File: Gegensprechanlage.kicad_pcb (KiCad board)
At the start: 2 copper layers, 42.2 x 31 mm, 13 parts, among them J1 To other, P1 22k, SW1 SW_Push, U1 LM386

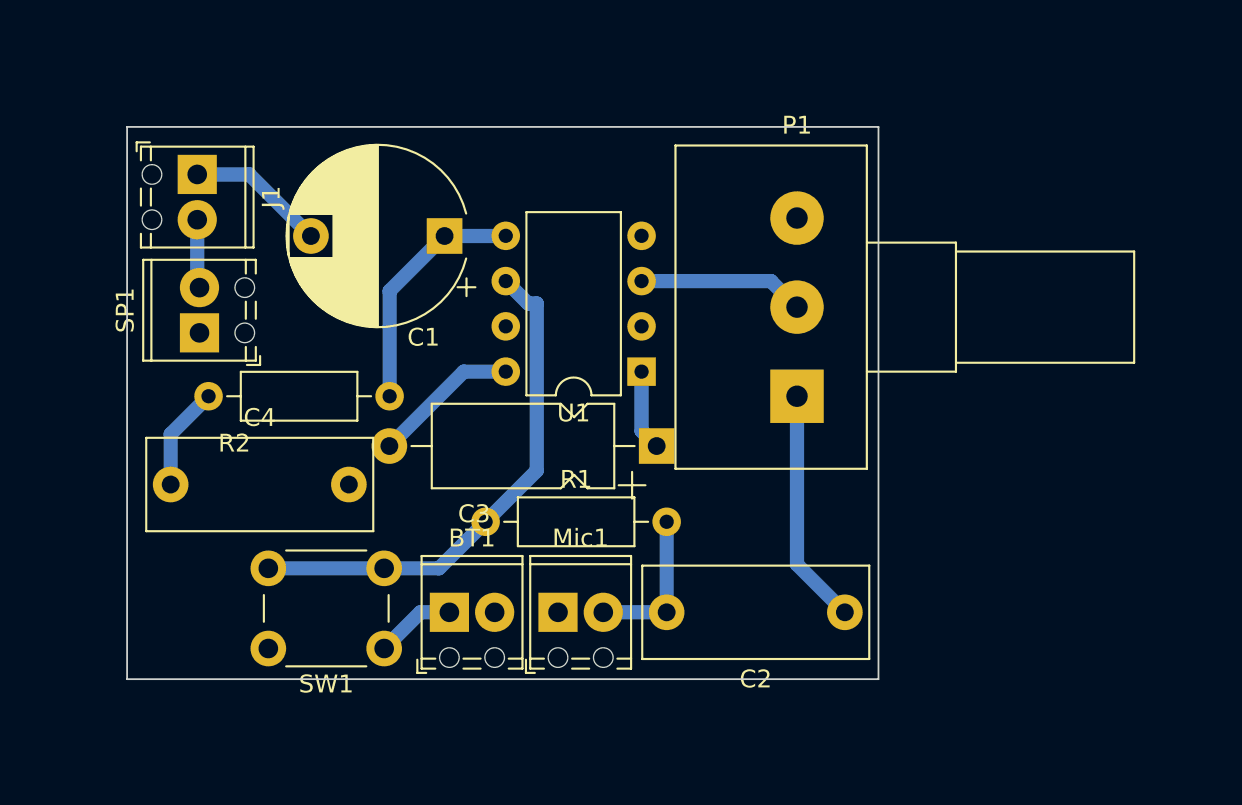
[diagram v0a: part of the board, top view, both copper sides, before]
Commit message: More compact layout
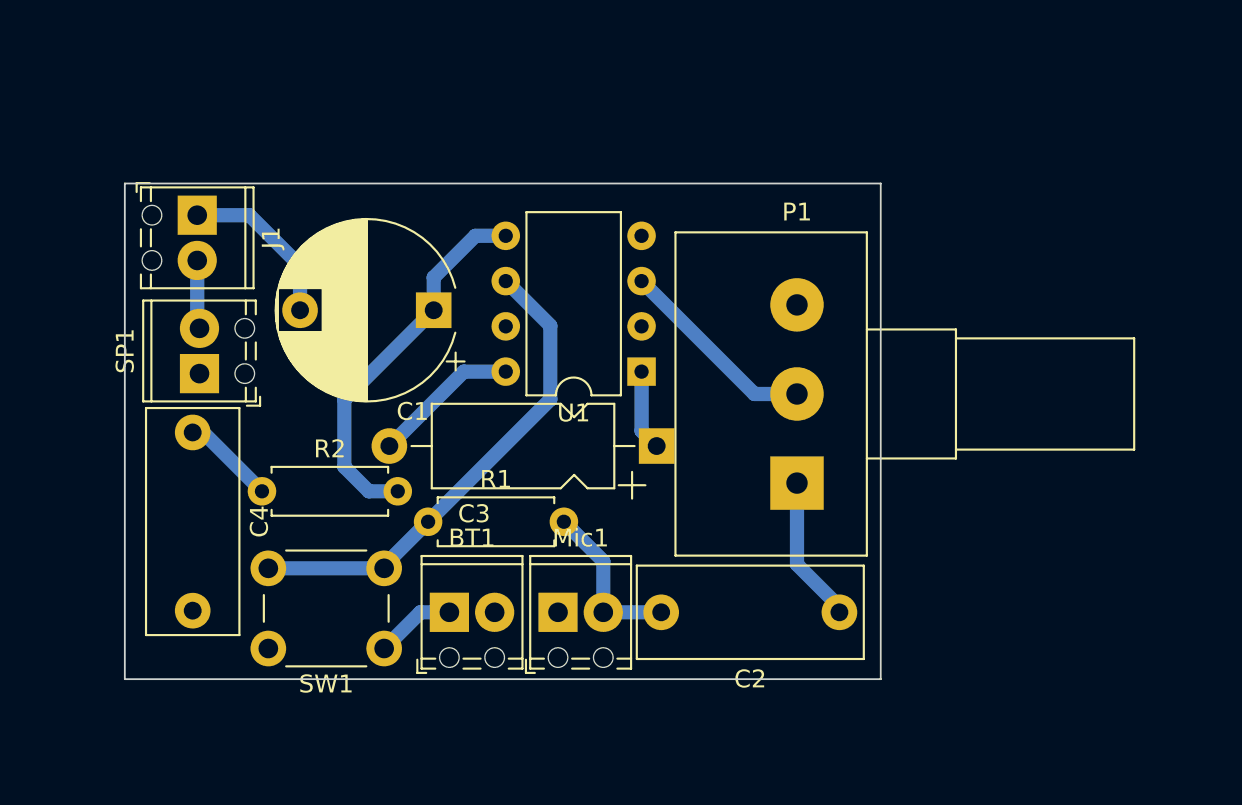
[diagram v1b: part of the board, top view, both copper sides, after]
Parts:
- R1, R2: footprint Resistor_THT:R_Axial_DIN0207_L6.3mm_D2.5mm_P10.16mm_Horizontal -> Resistor_THT:R_Axial_DIN0207_L6.3mm_D2.5mm_P7.62mm_Horizontal
- moved R2 6.12 mm to (91.9, 93.7)
- moved P1 4.87 mm to (121.9, 93.3)
- moved C1 4.21 mm to (101.5, 83.6)
- moved R1 3.23 mm to (101.2, 95.4)
- moved C4 3.17 mm to (88.0, 90.4), turned to -90 degrees
- moved J1 2.29 mm to (88.3, 78.2)
- moved SP1 2.29 mm to (88.4, 87.1)
- moved C2 0.31 mm to (124.3, 100.5)
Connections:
- net GND renamed Earth
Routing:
- net Net-(C1-Pad1): track 13.7 -> 21.3 mm
- net Net-(C2-Pad1): track 13.2 -> 8.36 mm
- net Net-(P1-Pad2): track 9.33 -> 11.3 mm
- net Net-(C1-Pad2): track 7.81 -> 9.44 mm
- net Net-(R1-Pad1): track 29.0 -> 27.5 mm
- net Net-(C2-Pad2): track 8.64 -> 9.55 mm
- net Net-(C4-Pad1): track 5.83 -> 5.25 mm
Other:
- board size 42.2 x 31 mm -> 42.4 x 27.8 mm

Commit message: Prepare for milling v1.0
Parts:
- added H1: MountingHole, MountingHole:MountingHole_2.7mm_M2.5, F.Cu at (127.5, 79.4)
- added H2: MountingHole, MountingHole:MountingHole_2.7mm_M2.5, F.Cu at (82.8, 101.8)
- added H3: MountingHole, MountingHole:MountingHole_2.7mm_M2.5, F.Cu at (82.8, 79.5)
- added H4: MountingHole, MountingHole:MountingHole_2.7mm_M2.5, F.Cu at (127.5, 101.8)
- 9V -: renamed from BT1; footprint TerminalBlock_Phoenix:TerminalBlock_Phoenix_MPT-0,5-2-2.54_1x02_P2.54mm_Horizontal -> TerminalBlock_Phoenix:TerminalBlock_Phoenix_PT-1,5-2-3.5-H_1x02_P3.50mm_Horizontal
- GND TX RX: renamed from J1; footprint TerminalBlock_Phoenix:TerminalBlock_Phoenix_MPT-0,5-2-2.54_1x02_P2.54mm_Horizontal -> TerminalBlock_Phoenix:TerminalBlock_Phoenix_PT-1,5-3-3.5-H_1x03_P3.50mm_Horizontal
- Mic -: renamed from Mic1; footprint TerminalBlock_Phoenix:TerminalBlock_Phoenix_MPT-0,5-2-2.54_1x02_P2.54mm_Horizontal -> TerminalBlock_Phoenix:TerminalBlock_Phoenix_PT-1,5-2-3.5-H_1x02_P3.50mm_Horizontal
- SP1: footprint TerminalBlock_Phoenix:TerminalBlock_Phoenix_MPT-0,5-2-2.54_1x02_P2.54mm_Horizontal -> TerminalBlock_Phoenix:TerminalBlock_Phoenix_PT-1,5-2-3.5-H_1x02_P3.50mm_Horizontal
- moved C2 14.9 mm to (117.5, 87.3), turned to -90 degrees
- moved GND TX RX 9.88 mm to (82.4, 86.2)
- moved SP1 8.13 mm to (91.2, 79.5), turned to 180 degrees
- moved Mic - 5.96 mm to (114.4, 101.2), turned to 180 degrees
- moved P1 5.47 mm to (126.9, 95.5)
- moved R1 2.34 mm to (103.5, 94.9)
- moved C4 1.54 mm to (88.2, 92.0)
- moved 9V - 1.12 mm to (103.3, 101.2)
- moved C3 0.77 mm to (113.3, 90.9)
- moved SW1 0.24 mm to (99.0, 102.5)
- moved C1 0.05 mm to (101.5, 83.5)
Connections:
- GND TX RX pad 1: Net-(C1-Pad2) -> Net-(J1-Pad1)
- GND TX RX pad 2: Net-(J1-Pad2) -> Net-(C1-Pad2)
- SP1 pad 2: Net-(J1-Pad2) -> Net-(J1-Pad1)
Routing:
- net Net-(J1-Pad1): track 0.00 -> 8.95 mm
- net Net-(BT1-Pad1): track 4.50 -> 11.6 mm
- net Net-(P1-Pad2): track 11.3 -> 17.3 mm
- net Net-(C1-Pad2): track 9.44 -> 14.2 mm
- net Net-(C2-Pad1): track 8.36 -> 12.8 mm
- net Net-(C2-Pad2): track 9.55 -> 13.8 mm
- net Net-(R1-Pad1): track 27.5 -> 31.5 mm
- net Net-(J1-Pad2): track 3.86 -> 0.00 mm
- net Net-(C1-Pad1): track 21.3 -> 23.1 mm
- net Net-(C4-Pad1): track 5.25 -> 4.19 mm
- net Net-(C3-Pad2): track 8.26 -> 8.97 mm
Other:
- board size 42.4 x 27.8 mm -> 51.5 x 28.6 mm
- board text added: "EARTH"
- board text added: "V1.0 - 9.12.22"
- board text removed: "V1.0 - 8.12.22"
